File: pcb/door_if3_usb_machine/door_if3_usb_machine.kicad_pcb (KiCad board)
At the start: 2 copper layers, 70 x 75 mm, 75 parts, among them J1 Conn_01x08, J2 Conn_02x05_Odd_Even, J3 Conn_01x08, Q1 IRF7343, Q2 IRF7343, Q3 IRF7343, Q4 IRF7343, Q5 IRF7343, Q6 IRF7343, U1 Pico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

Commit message: completed if3_usb_machine
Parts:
- D11, D13, D7, D9: moved to B.Cu
- moved R8 92.3 mm to (119.6, 73.6), turned to -90 degrees
- moved R6 86.2 mm to (128.4, 71.7), turned to 180 degrees
- moved R4 85.2 mm to (129.5, 69.8), turned to 180 degrees
- moved R3 83.6 mm to (140.0, 65.8), turned to 180 degrees
- moved JP1 75.4 mm to (123.6, 74.0), turned to 0 degrees
- moved R2 75.4 mm to (140.0, 71.1), turned to 180 degrees
- moved R25 71.9 mm to (145.5, 128.8), turned to -90 degrees
- moved R24 70.1 mm to (142.9, 128.8), turned to -90 degrees
- moved JP2 69.5 mm to (128.4, 74.0), turned to 0 degrees
- moved Q4 64.2 mm to (127.9, 125.5), turned to 90 degrees
- moved D8 61.7 mm to (121.0, 123.0), turned to 90 degrees
- moved D9 59.1 mm to (121.8, 123.0), turned to -90 degrees
- moved Q5 58.3 mm to (131.9, 117.1), turned to -90 degrees
- moved D10 55.0 mm to (123.8, 115.7), turned to 180 degrees
- moved D11 53.0 mm to (123.8, 114.9)
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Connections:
- J1 pad 5: unconnected-(J1-Pin_5-Pad5) -> OUT4
- J1 pad 6: unconnected-(J1-Pin_6-Pad6) -> OUT5
- J1 pad 7: unconnected-(J1-Pin_7-Pad7) -> OUT6
- J3 pad 5: OUT4 -> unconnected-(J3-Pin_5-Pad5)
- J3 pad 6: OUT5 -> unconnected-(J3-Pin_6-Pad6)
- J3 pad 7: OUT6 -> unconnected-(J3-Pin_7-Pad7)
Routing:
- net +24V: track 130.2 -> 214.6 mm, vias 5 -> 8
- net Net-(JP4-C): track 1.25 -> 65.3 mm, vias 1 -> 4
- net Net-(R5-Pad1): track 0.00 -> 56.1 mm, vias 0 -> 4
- net S_OUT6: track 0.00 -> 34.7 mm
- net S_OUT4: track 0.00 -> 31.7 mm
- net S_OUT5: track 0.00 -> 28.5 mm, vias 0 -> 4
- net OUT6: track 0.00 -> 27.2 mm, vias 0 -> 1
- net OUT5: track 0.00 -> 24.7 mm, vias 0 -> 1
- net S_IN1: track 0.00 -> 23.7 mm, vias 0 -> 2
- net unconnected-(U1-GPIO10-Pad14): track 22.9 -> 0.00 mm
- net Net-(JP10-C): track 2.06 -> 22.8 mm
- net IN2: track 9.77 -> 30.4 mm, vias 0 -> 2
- net OUT4: track 0.00 -> 20.5 mm, vias 0 -> 1
- net OUT3: track 0.00 -> 18.7 mm, vias 0 -> 1
- net S_OUT3: track 0.00 -> 18.2 mm
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- added copper zone on F.Cu, net OUT4
- added copper zone on F.Cu, net OUT5
- added copper zone on F.Cu, net OUT6

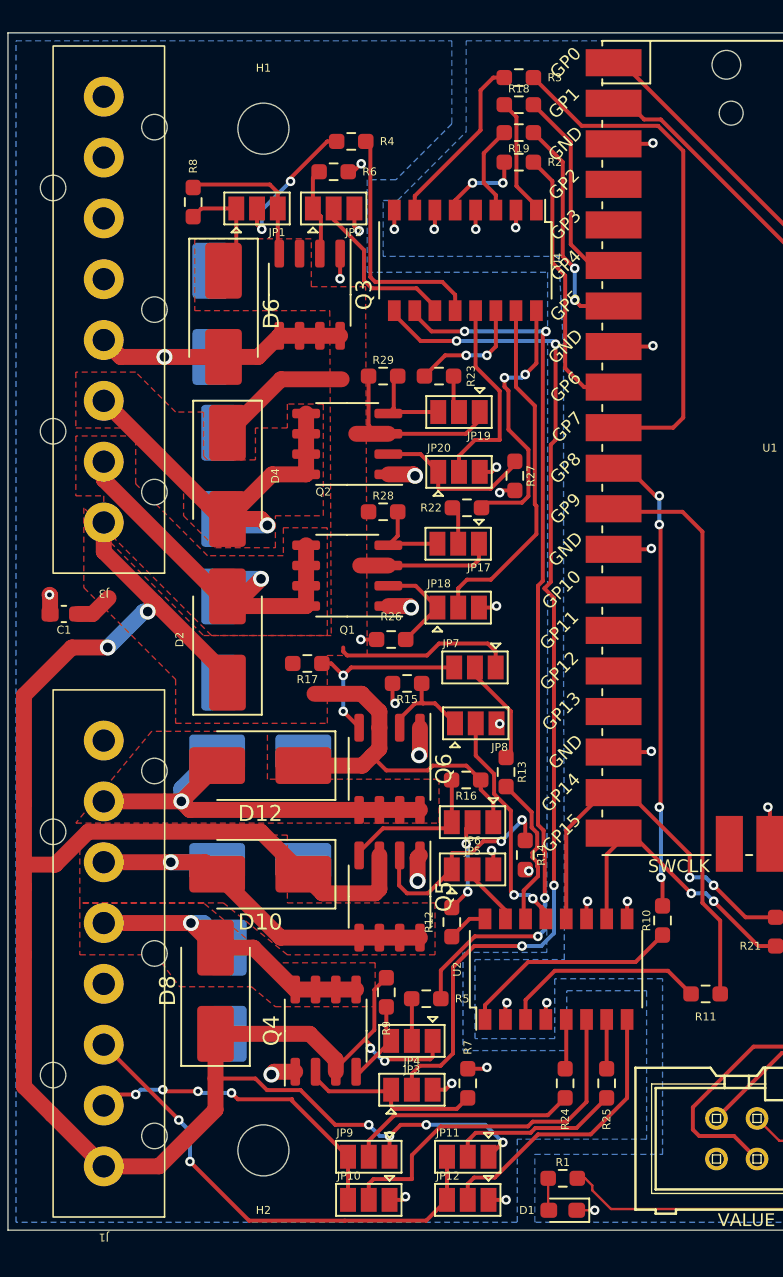
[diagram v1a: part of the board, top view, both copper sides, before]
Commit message: finalized if3_usb_machine pcb
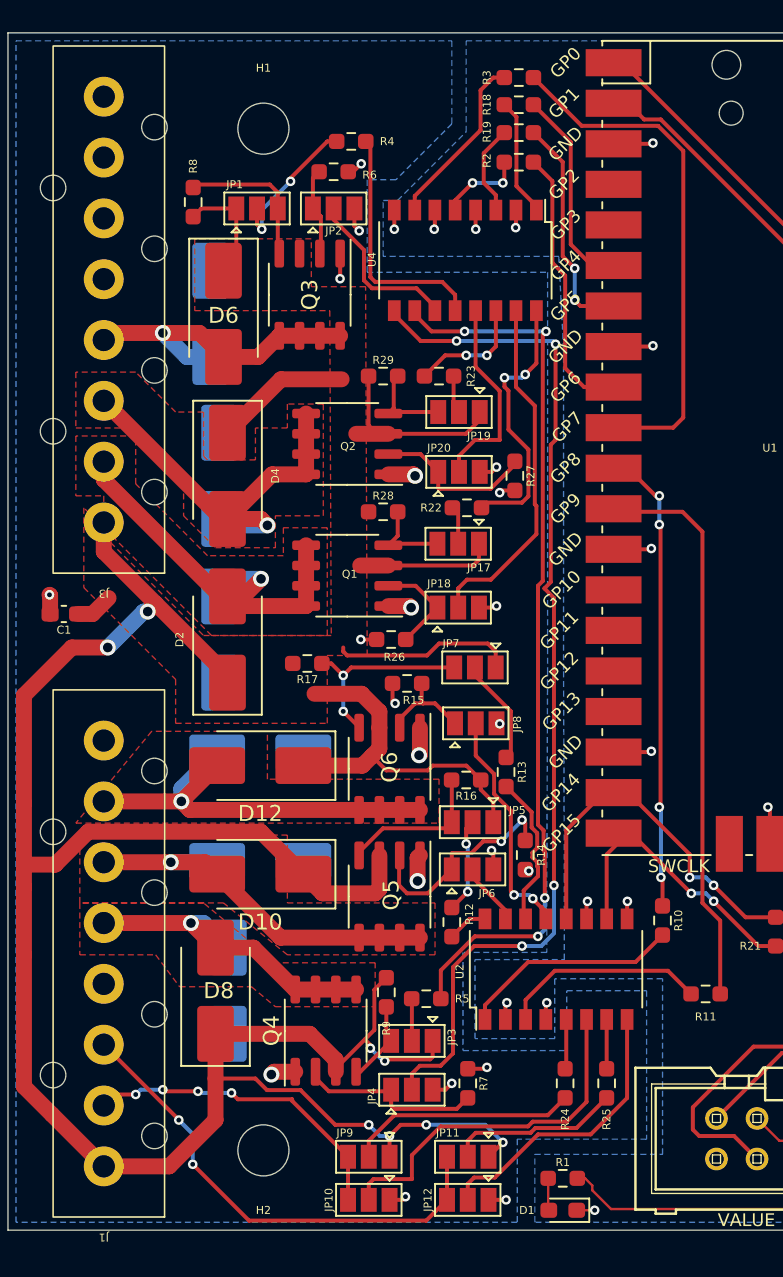
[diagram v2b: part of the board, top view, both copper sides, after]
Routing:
- net OUT3: track 18.7 -> 19.8 mm
